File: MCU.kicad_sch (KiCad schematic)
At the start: 1 part, among them U2 CC2640R2FRSMR

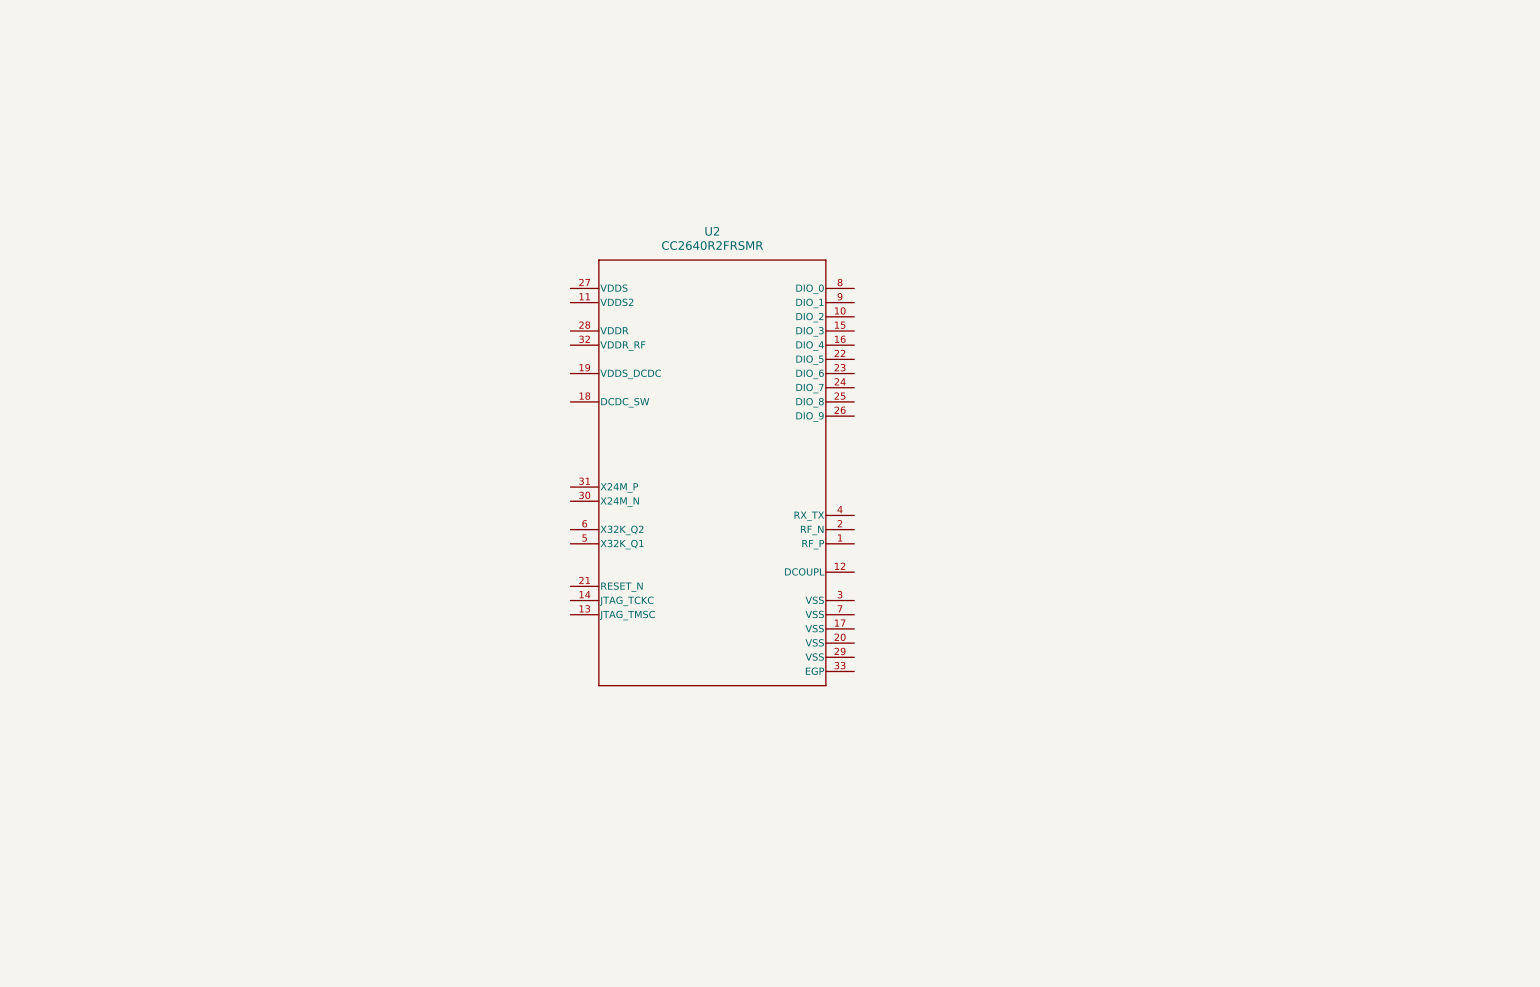
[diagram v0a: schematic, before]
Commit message: first finished schematic version of the MCU as well as sensor. starting out with schematic of the power related components
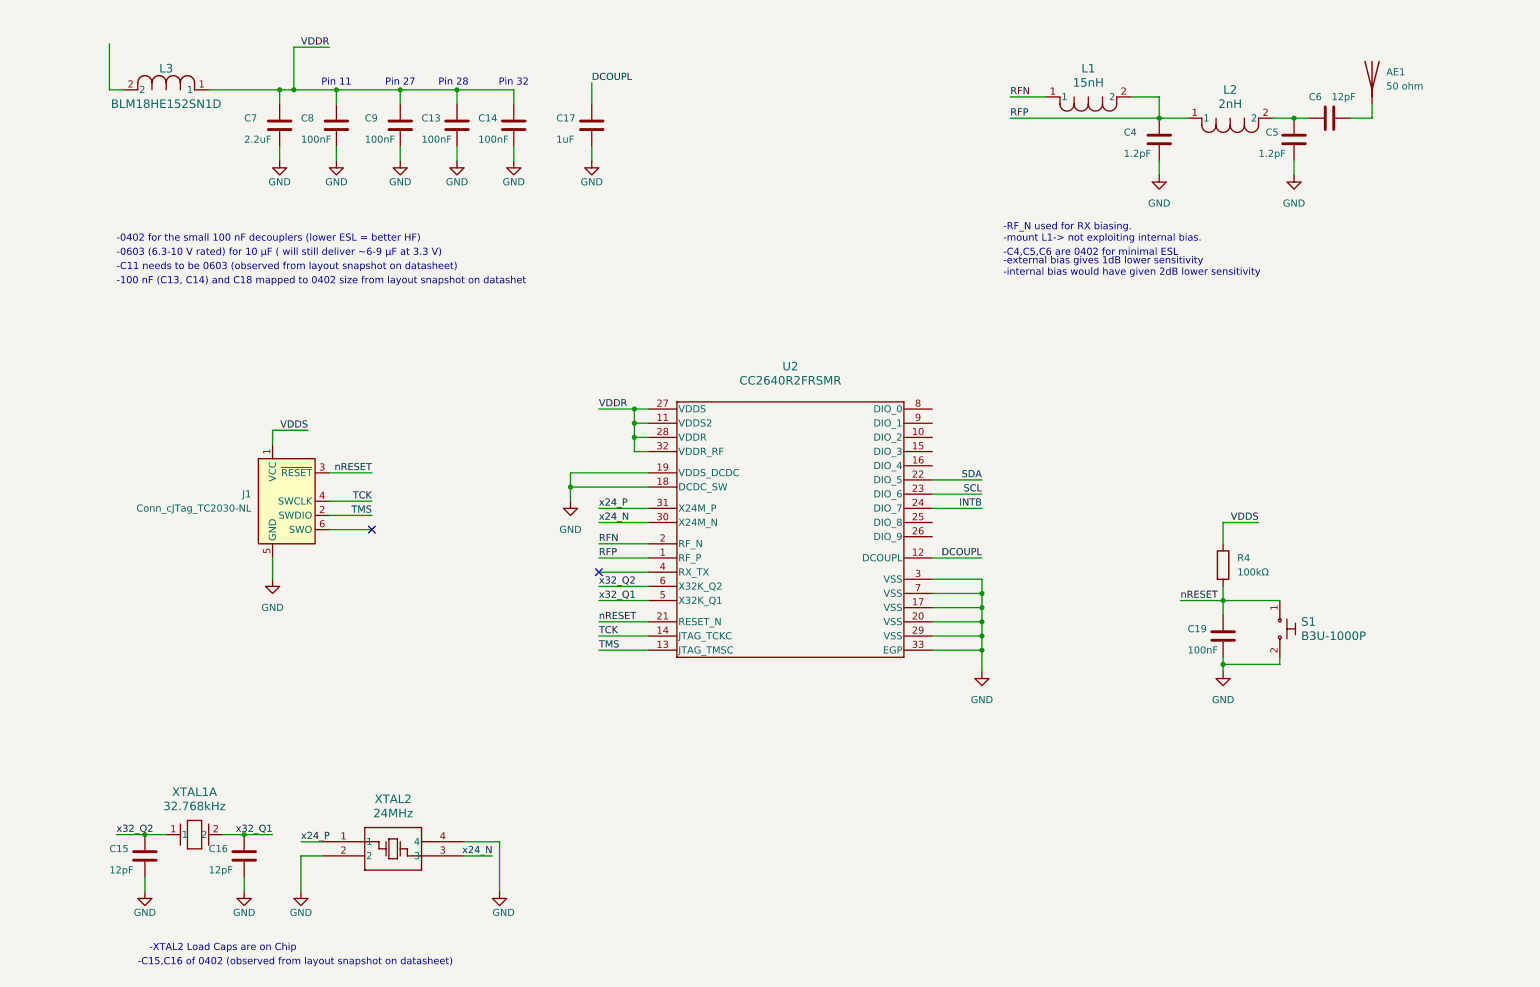
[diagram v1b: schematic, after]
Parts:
- added AE1: 50 ohm, symbol antenna_local:Antenna
- added C13, C14, C19, C8, C9: 100nF, symbol unpolarizedcapacitor:C
- added C15, C16, C6: 12pF, symbol unpolarizedcapacitor:C
- added C17: 1uF, symbol unpolarizedcapacitor:C
- added C4, C5: 1.2pF, symbol unpolarizedcapacitor:C
- added C7: 2.2uF, symbol unpolarizedcapacitor:C
- added J1: Conn_cJTag_TC2030-NL, connectorTagConnect_local:Tag-Connect_TC2030-IDC-NL_2x03_P1.27mm_Vertical, symbol cJTAG_Connector_local:Conn_ARM_SWD_TagConnect_TC2030-NL
- added L1: 15nH, IND_LQG15HN_02_MUR, symbol 15nH_inductor_local:LQG15HS15NJ02D
- added L2: 2nH, IND_LQG15_MUR, symbol 2nH_inductor_local:LQG15HS2N0S02D
- added L3: BLM18HE152SN1D, IND_BLM18_0603_MUR, symbol ul_ferrite_bead_local:BLM18HE152SN1D
- added R4: 100kΩ, symbol resistor:R
- added S1: B3U-1000P, dk_tactileSwitch_B3U1000P_local:Switch_Tactile_SMD_B3U-1000P, symbol dk_Tactile-Switches_local:B3U-1000P
- added XTAL1: 32.768kHz, XTAL_SC-20S_EPS, symbol ul_crystal32768_SC20S-12-5PF20PPM_local:SC20S-12.5PF20PPM
- added XTAL2: 24MHz, ECS-160-8-36-RHN-TR_ECS, symbol ul_24Mcrystal_ESC-240-8-36-RWN-TR_local:ECS-240-8-36-RWN-TR
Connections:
- net RFP: now reaches U2.1 (RF_P)
- net RFP: now also C4.1, L1.2, L2.1
- net VDDR: now reaches U2.11 (VDDS2)
- net VDDR: now also U2.27 (VDDS), U2.28 (VDDR), U2.32 (VDDR_RF), C13.1, C14.1, C7.1, C8.1, C9.1, L3.1
- net DCOUPL: now reaches U2.12 (DCOUPL)
- net DCOUPL: now also C17.1
- net TMS: now reaches U2.13 (JTAG_TMSC)
- net TMS: now also J1.2 (SWDIO)
- net TCK: now reaches U2.14 (JTAG_TCKC)
- net TCK: now also J1.4 (SWCLK)
- net GND: now reaches U2.17 (VSS)
- net GND: now also U2.18 (DCDC_SW), U2.19 (VDDS_DCDC), U2.20 (VSS), U2.29 (VSS), U2.3 (VSS), U2.33 (EGP), U2.7 (VSS), C13.2, C14.2, C15.2, C16.2, C17.2, C19.2, C4.2, C5.2, C7.2, C8.2, C9.2, J1.5 (GND), S1.2, XTAL2.2, XTAL2.4
- net RFN: now reaches U2.2 (RF_N)
- net RFN: now also L1.1
- net nRESET: now reaches U2.21 (RESET_N)
- net nRESET: now also C19.1, J1.3 (~{RESET}), R4.2, S1.1
- net SDA: now reaches U2.22 (DIO_5)
- net SCL: now reaches U2.23 (DIO_6)
- net INTB: now reaches U2.24 (DIO_7)
- net x24_N: now reaches U2.30 (X24M_N)
- net x24_N: now also XTAL2.3
- net x24_P: now reaches U2.31 (X24M_P)
- net x24_P: now also XTAL2.1
- net x32_Q1: now reaches U2.5 (X32K_Q1)
- net x32_Q1: now also C16.1, XTAL1.2
- net x32_Q2: now reaches U2.6 (X32K_Q2)
- net x32_Q2: now also C15.1, XTAL1.1
- new net: C5.1, C6.1, L2.2
- new net: AE1.1 (A), C6.2
- new net VDDS: J1.1 (VCC), R4.1
- no-connect marks 0 -> 2
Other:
- note added: "-0402 for the small 100 nF decouplers (lower ESL = better HF)"
- note added: "-0603 (6.3-10 V rated) for 10 µF ( will still deliver ~6-9 µF at 3.3 V)"
- note added: "-100 nF (C13, C14) and C18 mapped to 0402 size from layout snapshot on datashet"
- note added: "-C11 needs to be 0603 (observed from layout snapshot on datasheet)"
- note added: "-C15,C16 of 0402 (observed from layout snapshot on datasheet)"
- note added: "-C4,C5,C6 are 0402 for minimal ESL"
- note added: "-RF_N used for RX biasing. -mount L1-> not exploiting internal bias."
- note added: "-XTAL2 Load Caps are on Chip"
- note added: "-external bias gives 1dB lower sensitivity -internal bias would have given 2dB lower sensitivity"
- note added: "Pin 11"
- note added: "Pin 27"
- note added: "Pin 28"
- note added: "Pin 32"

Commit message: done with first version PowerSection of LoTiBloxy plus MCU plus sensor sheets. still have to add meaningfull comments to all schematic components. still have to make sure every symbol is associated to footprint. still have to perform ERC on what implemented.
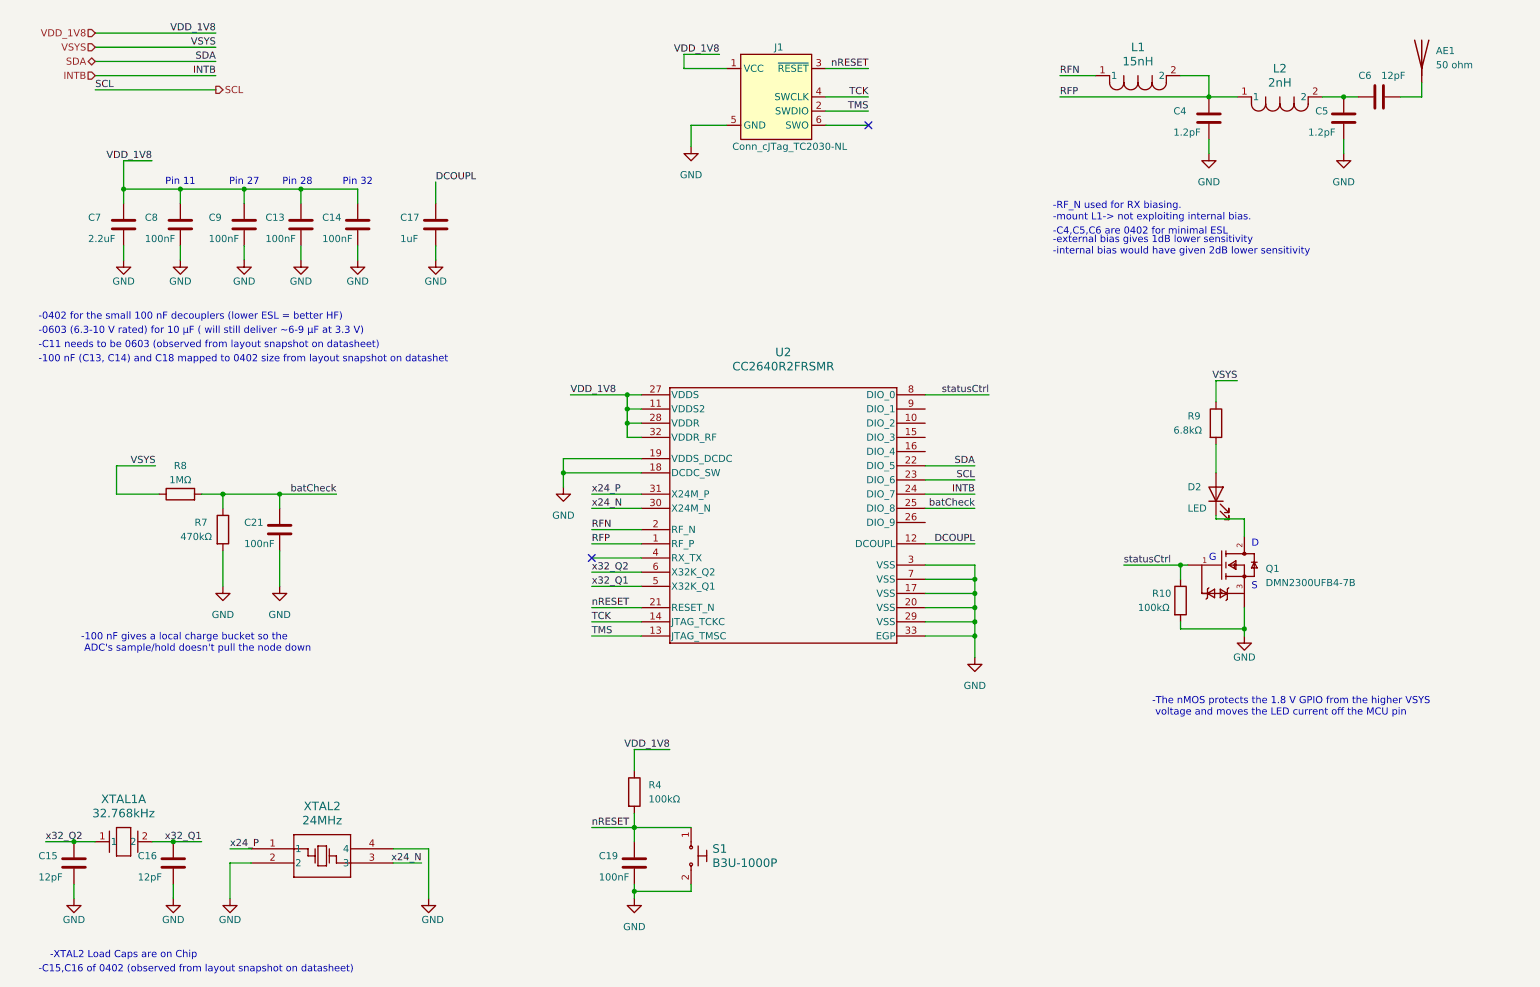
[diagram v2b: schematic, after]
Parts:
- removed L3: BLM18HE152SN1D, IND_BLM18_0603_MUR, symbol ul_ferrite_bead_local:BLM18HE152SN1D
- added C21: 100nF, symbol unpolarizedcapacitor:C
- added D2: LED, symbol LED_local:LED
- added Q1: DMN2300UFB4-7B, nmos_DMN2300UFB4_local:Diodes_Inc.-X2-DFN1006-3-04_2017-0-MFG, symbol nmos_DMN2300UFB4_local:DMN2300UFB4-7B
- added R10: 100kΩ, symbol resistor:R
- added R7: 470kΩ, symbol resistor:R
- added R8: 1MΩ, symbol resistor:R
- added R9: 6.8kΩ, symbol resistor:R
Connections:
- net VDDS is gone; now on net VDD_1V8: J1.1 (VCC), R4.1
- net GND: now also C21.2, Q1.3 (S), R10.2, R7.2
- net batCheck: now reaches U2.25 (DIO_8)
- net batCheck: now also C21.1, R7.1, R8.2
- net statusCtrl: now reaches U2.8 (DIO_0)
- net statusCtrl: now also Q1.1 (G), R10.1
- net VDDR renamed VDD_1V8
- new net: D2.2 (A), R9.2
- new net: D2.1 (K), Q1.2 (D)
- new net VSYS: R8.1, R9.1
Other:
- note added: "-100 nF gives a local charge bucket so the ADC's sample/hold doesn't pull the node down"
- note added: "-The nMOS protects the 1.8 V GPIO from the higher VSYS voltage and moves the LED current off the MCU pin"
- note added: "D"
- note added: "G"
- note added: "S"
- moved on the sheet: AE1, C13, C14, C15, C16, C17, C19, C4, C5, C6, C7, C8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
